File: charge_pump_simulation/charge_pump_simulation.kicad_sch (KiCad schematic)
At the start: 23 parts, among them Q1 IRLML6402, Q2 IRLML2402, Q3 BC847

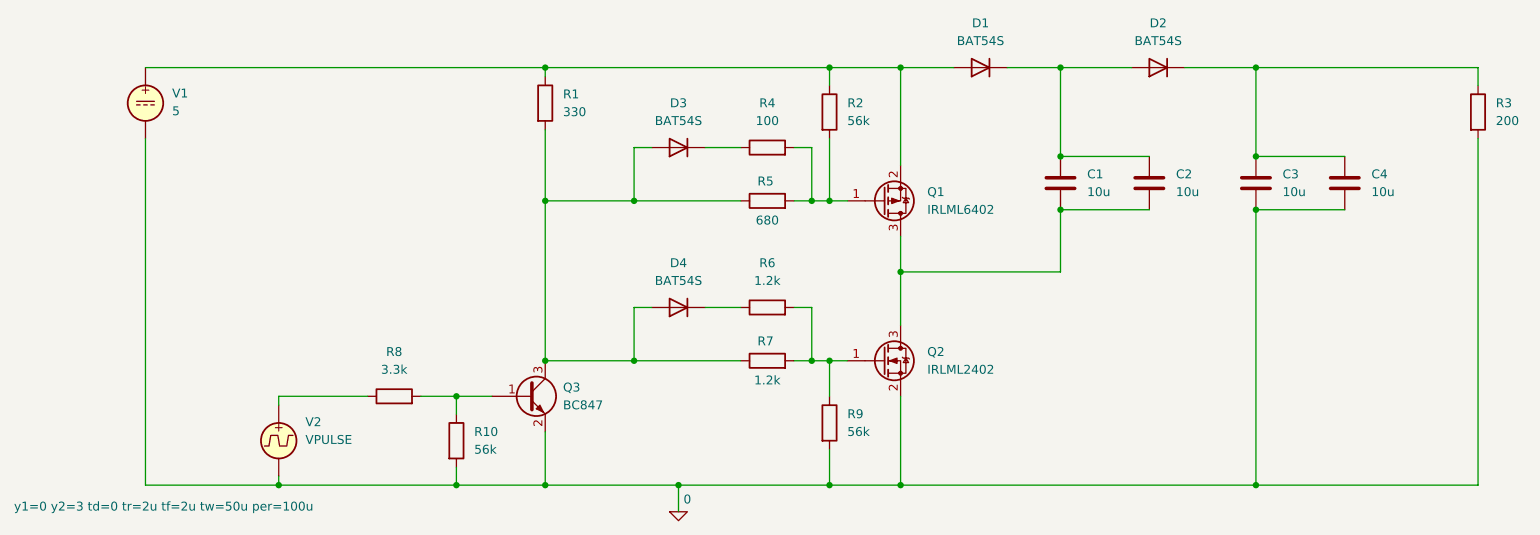
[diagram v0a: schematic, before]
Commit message: Tune FETs switchng times and frequency
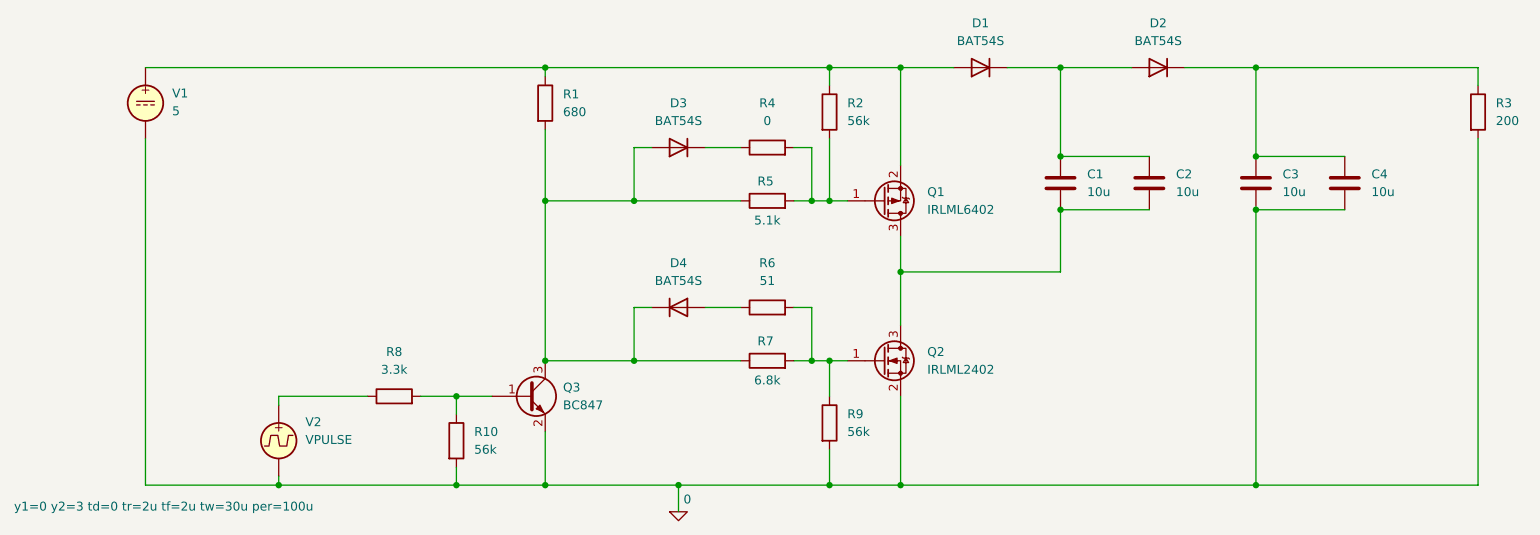
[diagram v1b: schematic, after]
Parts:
- R1: value 330 -> 680
- R4: value 100 -> 0
- R5: value 680 -> 5.1k
- R6: value 1.2k -> 51
- R7: value 1.2k -> 6.8k
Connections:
- net at R6.1: now also D4.2 (A); no longer D4.1 (K)
- net at D3.2 (A), Q3.3 (C), R1.2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: now also D4.1 (K); no longer D4.2 (A)
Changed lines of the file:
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@@
 			)
 		)
-		(property "Value" "1.2k"
+		(property "Value" "51"
 			(at 152.4 93.98 90)
 			(effects
@@
 			)
 		)
-		(property "Value" "330"
+		(property "Value" "680"
 			(at 123.19 69.8499 0)
 			(effects
@@
 			)
 		)
-		(property "Value" "680"
+		(property "Value" "5.1k"
 			(at 152.4 85.344 90)
 			(effects
@@
 				(path "/598be1a0-ca1b-471b-9bdc-3f62a20c50cf"
 					(reference "R5")
+					(unit 1)
+				)
+			)
+		)
+	)
+	(symbol
+		(lib_id "Device:D")
+		(at 139.7 97.79 0)
+		(unit 1)
+		(exclude_from_sim no)
+		(in_bom yes)
+		(on_board yes)
+		(dnp no)
+		(fields_autoplaced yes)
+		(property "Reference" "D4"
+			(at 139.7 91.44 0)
+			(effects
+				(font
+					(size 1.27 1.27)
+				)
+			)
+		)
+		(property "Value" "BAT54S"
+			(at 139.7 93.98 0)
+			(effects
+				(font
+					(size 1.27 1.27)
+				)
+			)
+		)
+		(property "Footprint" ""
+			(at 139.7 97.79 0)
+			(effects
+				(font
+					(size 1.27 1.27)
+				)
+				(hide yes)
+			)
+		)
+		(property "Datasheet" "~"
+			(at 139.7 97.79 0)
+			(effects
+				(font
+					(size 1.27 1.27)
+				)
+				(hide yes)
+			)
+		)
+		(property "Description" "Diode"
+			(at 139.7 97.79 0)
+			(effects
+				(font
+					(size 1.27 1.27)
+				)
+				(hide yes)
+			)
+		)
+		(property "Sim.Device" "D"
+			(at 139.7 97.79 0)
+			(effects
+				(font
+					(size 1.27 1.27)
+				)
+				(hide yes)
+			)
+		)
+		(property "Sim.Pins" "1=K 2=A"
+			(at 139.7 97.79 0)
+			(effects
+				(font
+					(size 1.27 1.27)
+				)
+				(hide yes)
+			)
+		)
+		(property "Sim.Library" "models/bat54s.lib"
+			(at 139.7 97.79 0)
+			(effects
+				(font
+					(size 1.27 1.27)
+				)
+				(hide yes)
+			)
+		)
+		(property "Sim.Name" "BAT54"
+			(at 139.7 97.79 0)
+			(effects
+				(font
+					(size 1.27 1.27)
+				)
+				(hide yes)
+			)
+		)
+		(pin "2"
+		)
+		(pin "1"
+		)
+		(instances
+			(project "charge_pump_simulation"
+				(path "/598be1a0-ca1b-471b-9bdc-3f62a20c50cf"
+					(reference "D4")
 					(unit 1)
 				)
@@
 	)
 	(symbol
-		(lib_id "Device:D")
-		(at 139.7 97.79 180)
-		(unit 1)
-		(exclude_from_sim no)
-		(in_bom yes)
-		(on_board yes)
-		(dnp no)
-		(fields_autoplaced yes)
-		(property "Reference" "D4"
-			(at 139.7 91.44 0)
-			(effects
-				(font
-					(size 1.27 1.27)
-				)
-			)
-		)
-		(property "Value" "BAT54S"
-			(at 139.7 93.98 0)
-			(effects
-				(font
-					(size 1.27 1.27)
-				)
-			)
-		)
-		(property "Footprint" ""
-			(at 139.7 97.79 0)
-			(effects
-				(font
-					(size 1.27 1.27)
-				)
-				(hide yes)
-			)
-		)
-		(property "Datasheet" "~"
-			(at 139.7 97.79 0)
-			(effects
-				(font
-					(size 1.27 1.27)
-				)
-				(hide yes)
-			)
-		)
-		(property "Description" "Diode"
-			(at 139.7 97.79 0)
-			(effects
-				(font
-					(size 1.27 1.27)
-				)
-				(hide yes)
-			)
-		)
-		(property "Sim.Device" "D"
-			(at 139.7 97.79 0)
-			(effects
-				(font
-					(size 1.27 1.27)
-				)
-				(hide yes)
-			)
-		)
-		(property "Sim.Pins" "1=K 2=A"
-			(at 139.7 97.79 0)
-			(effects
-				(font
-					(size 1.27 1.27)
-				)
-				(hide yes)
-			)
-		)
-		(property "Sim.Library" "models/bat54s.lib"
-			(at 139.7 97.79 0)
-			(effects
-				(font
-					(size 1.27 1.27)
-				)
-				(hide yes)
-			)
-		)
-		(property "Sim.Name" "BAT54"
-			(at 139.7 97.79 0)
-			(effects
-				(font
-					(size 1.27 1.27)
-				)
-				(hide yes)
-			)
-		)
-		(pin "2"
-		)
-		(pin "1"
-		)
-		(instances
-			(project "charge_pump_simulation"
-				(path "/598be1a0-ca1b-471b-9bdc-3f62a20c50cf"
-					(reference "D4")
-					(unit 1)
-				)
-			)
-		)
-	)
-	(symbol
 		(lib_id "Device:C")
 		(at 234.95 80.01 0)
@@
 			)
 		)
-		(property "Value" "100"
+		(property "Value" "0"
 			(at 152.4 71.12 90)
 			(effects
@@
 			)
 		)
-		(property "Value" "1.2k"
+		(property "Value" "6.8k"
 			(at 152.4 108.204 90)
 			(effects
@@
 			)
 		)
-		(property "Sim.Params" "y1=0 y2=3 td=0 tr=2u tf=2u tw=50u per=100u"
+		(property "Sim.Params" "y1=0 y2=3 td=0 tr=2u tf=2u tw=30u per=100u"
 			(at 44.704 126.238 0)
 			(effects
